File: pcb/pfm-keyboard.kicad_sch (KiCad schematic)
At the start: 54 parts, among them U2 ssd1306-display

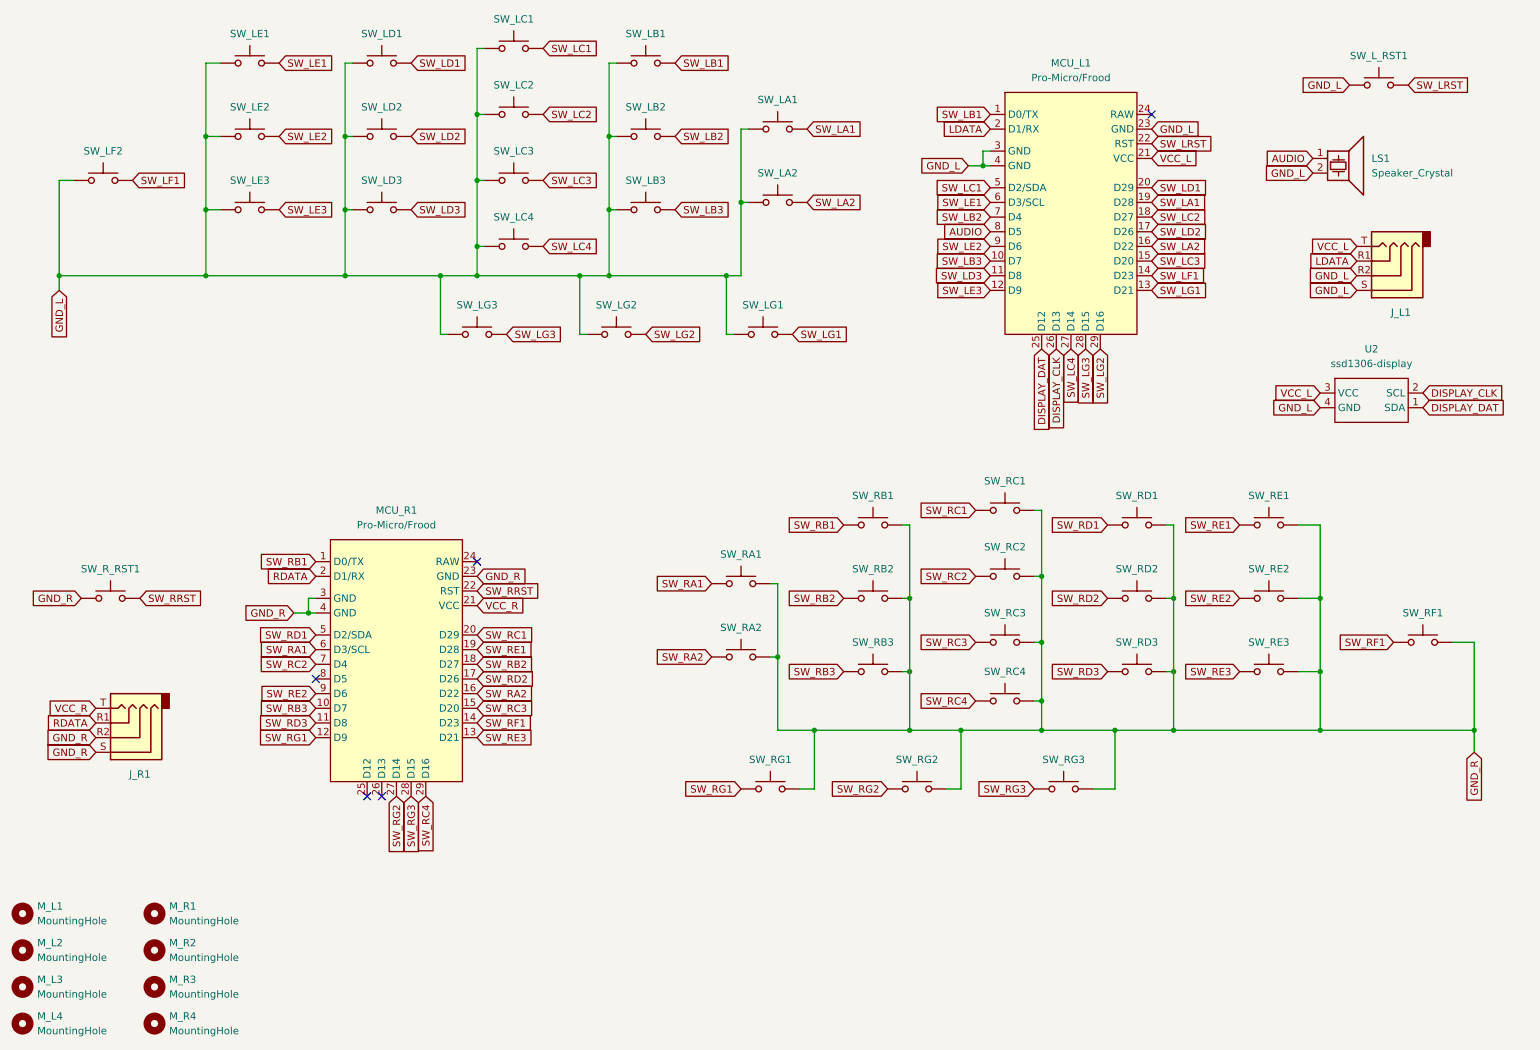
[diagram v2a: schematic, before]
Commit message: Version 4 - better key placement, same pin usage on left and right, added test points
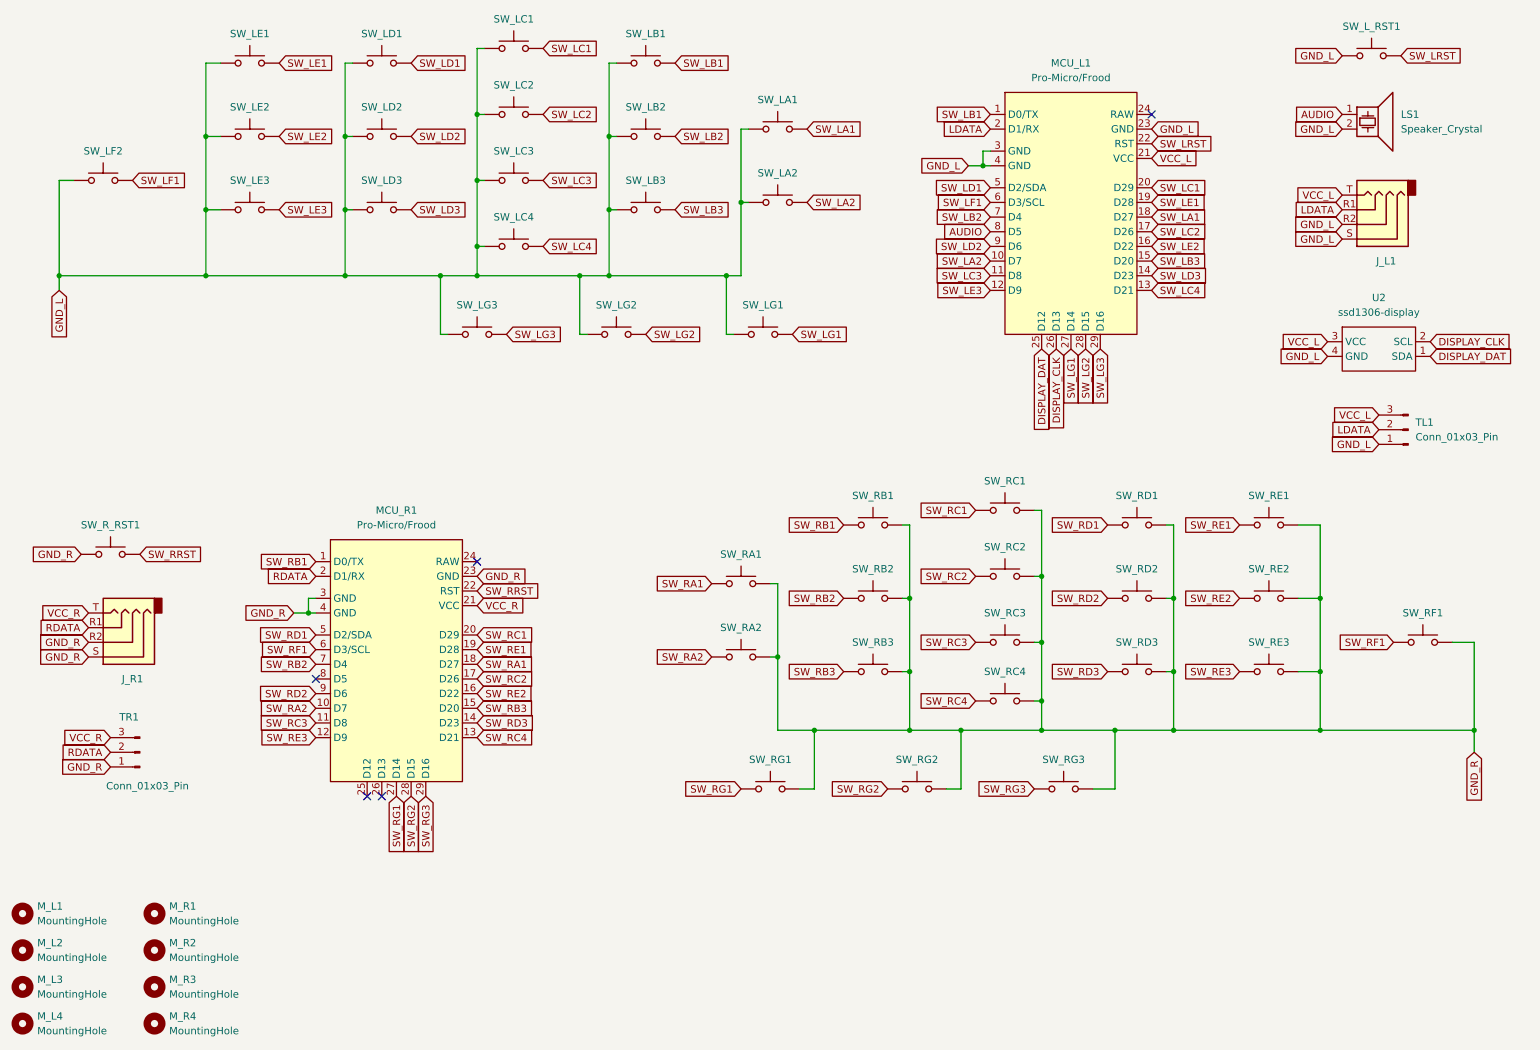
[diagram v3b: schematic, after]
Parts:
- added TL1, TR1: Conn_01x03_Pin, Connector_PinHeader_2.54mm:PinHeader_1x03_P2.54mm_Vertical, symbol Connector:Conn_01x03_Pin
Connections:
- net GND_L: now also TL1.1 (Pin_1)
- net GND_R: now also TR1.1 (Pin_1)
- net LDATA: now also TL1.2 (Pin_2)
- net RDATA: now also TR1.2 (Pin_2)
- net SW_LA1: now also MCU_L1.18 (D27); no longer MCU_L1.19 (D28)
- net SW_LA2: now also MCU_L1.10 (D7); no longer MCU_L1.16 (D22)
- net SW_LB3: now also MCU_L1.15 (D20); no longer MCU_L1.10 (D7)
- net SW_LC1: now also MCU_L1.20 (D29); no longer MCU_L1.5 (D2/SDA)
- net SW_LC2: now also MCU_L1.17 (D26); no longer MCU_L1.18 (D27)
- net SW_LC3: now also MCU_L1.11 (D8); no longer MCU_L1.15 (D20)
- net SW_LC4: now also MCU_L1.13 (D21); no longer MCU_L1.27 (D14)
- net SW_LD1: now also MCU_L1.5 (D2/SDA); no longer MCU_L1.20 (D29)
- net SW_LD2: now also MCU_L1.9 (D6); no longer MCU_L1.17 (D26)
- net SW_LD3: now also MCU_L1.14 (D23); no longer MCU_L1.11 (D8)
- net SW_LE1: now also MCU_L1.19 (D28); no longer MCU_L1.6 (D3/SCL)
- net SW_LE2: now also MCU_L1.16 (D22); no longer MCU_L1.9 (D6)
- net SW_LF1: now also MCU_L1.6 (D3/SCL); no longer MCU_L1.14 (D23)
- net SW_LG1: now also MCU_L1.27 (D14); no longer MCU_L1.13 (D21)
- net SW_LG2: now also MCU_L1.28 (D15); no longer MCU_L1.29 (D16)
- net SW_LG3: now also MCU_L1.29 (D16); no longer MCU_L1.28 (D15)
- net SW_RA1: now also MCU_R1.18 (D27); no longer MCU_R1.6 (D3/SCL)
- net SW_RA2: now also MCU_R1.10 (D7); no longer MCU_R1.16 (D22)
- net SW_RB2: now also MCU_R1.7 (D4); no longer MCU_R1.18 (D27)
- net SW_RB3: now also MCU_R1.15 (D20); no longer MCU_R1.10 (D7)
- net SW_RC2: now also MCU_R1.17 (D26); no longer MCU_R1.7 (D4)
- net SW_RC3: now also MCU_R1.11 (D8); no longer MCU_R1.15 (D20)
- net SW_RC4: now also MCU_R1.13 (D21); no longer MCU_R1.29 (D16)
- net SW_RD2: now also MCU_R1.9 (D6); no longer MCU_R1.17 (D26)
- net SW_RD3: now also MCU_R1.14 (D23); no longer MCU_R1.11 (D8)
- net SW_RE2: now also MCU_R1.16 (D22); no longer MCU_R1.9 (D6)
- net SW_RE3: now also MCU_R1.12 (D9); no longer MCU_R1.13 (D21)
- net SW_RF1: now also MCU_R1.6 (D3/SCL); no longer MCU_R1.14 (D23)
- net SW_RG1: now also MCU_R1.27 (D14); no longer MCU_R1.12 (D9)
- net SW_RG2: now also MCU_R1.28 (D15); no longer MCU_R1.27 (D14)
- net SW_RG3: now also MCU_R1.29 (D16); no longer MCU_R1.28 (D15)
- net VCC_L: now also TL1.3 (Pin_3)
- net VCC_R: now also TR1.3 (Pin_3)
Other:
- moved on the sheet: J_L1, J_R1, LS1, SW_L_RST1, SW_R_RST1, U2
